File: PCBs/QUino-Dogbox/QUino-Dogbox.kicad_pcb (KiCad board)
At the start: 2 copper layers, 77.5 x 64.8 mm, 70 parts, among them IC1 TP5000-QFN16, J1 RFID RC522, J2 Micro_SD_Card, J3 Neopixel, J4 USB_B_Micro, J5 Conn_01x07_Male, Q1 Q12MHz/20pF/10ppm/4P/3.2x2.5mm, Q2 BC817-40(SOT23), Q3 BC817-40(SOT23), Q4 SI2302DS NMOS/GSD, Q5 QBC817 NPN/BEC, U1 ESP32-S2-WROVER, U3 CH340T(SSOP20W), U4 AMS1117-3.3

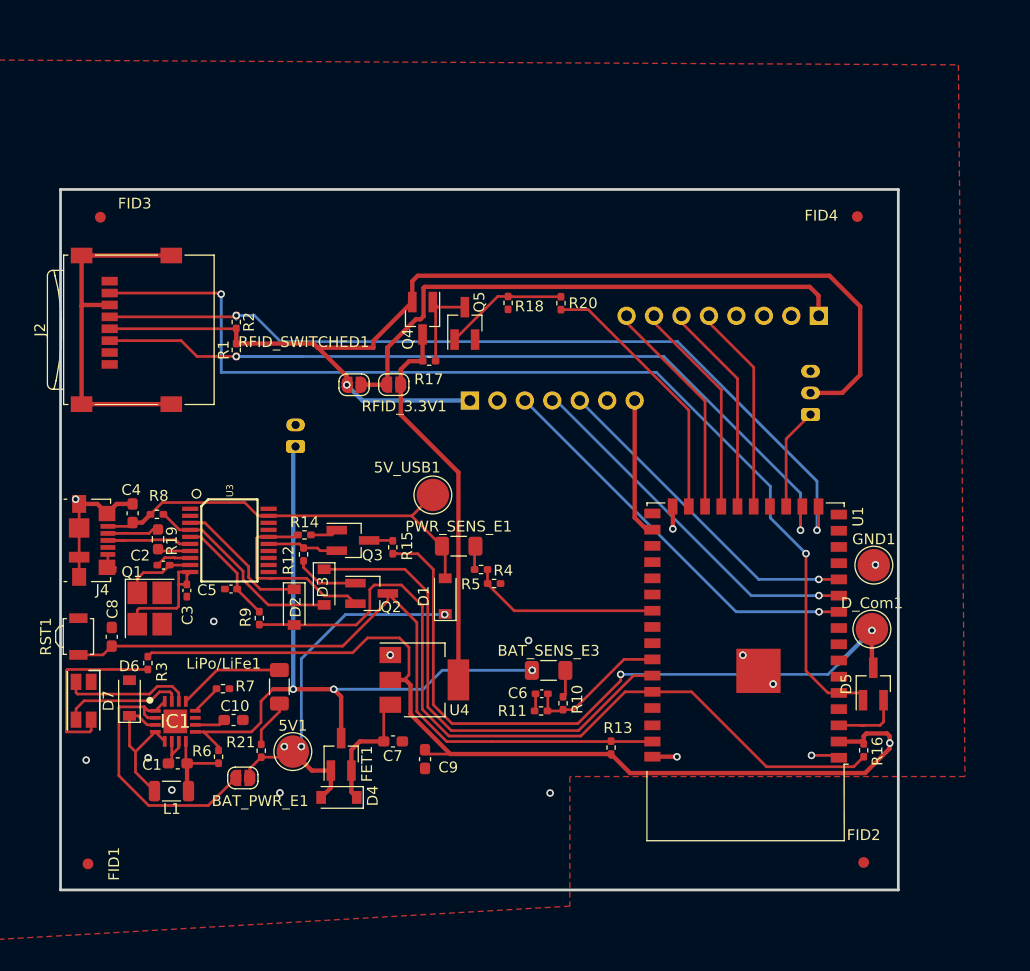
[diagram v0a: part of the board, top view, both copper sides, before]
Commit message: Update ESP32 to WROVER-B
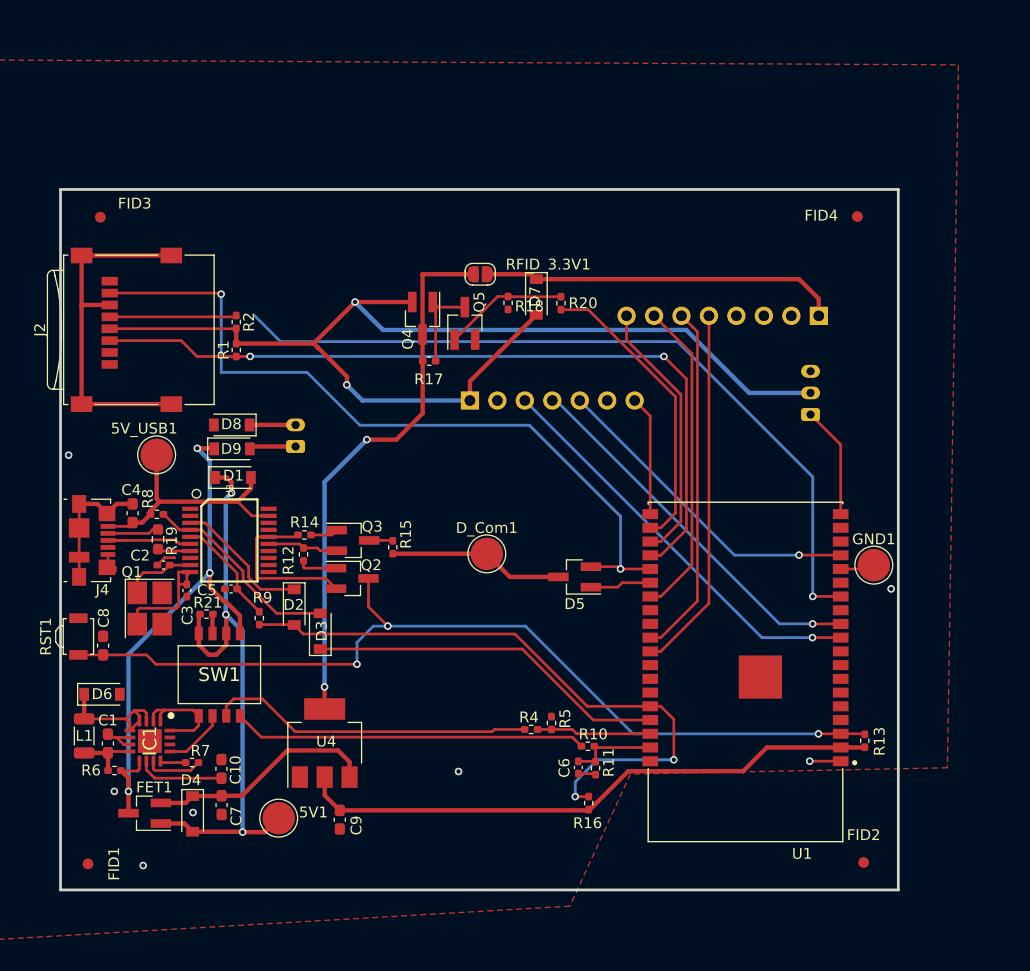
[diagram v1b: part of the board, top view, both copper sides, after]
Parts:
- removed BAT_PWR_E1, RFID_SWITCHED1: Opened, Jumper:SolderJumper-2_P1.3mm_Open_RoundedPad1.0x1.5mm
- removed BAT_SENS_E3, LiPo/LiFe1, PWR_SENS_E1: Opened, Resistor_SMD:R_1206_3216Metric_Pad1.30x1.75mm_HandSolder
- removed R3: 1k/R0402, Resistor_SMD:R_0402_1005Metric_Pad0.72x0.64mm_HandSolder
- added D8: 1N5819W/SOD123, Diode_SMD:D_SOD-123, F.Cu at (102.8, 98.5)
- added D9: 1N5819W/SOD123, Diode_SMD:D_SOD-123, F.Cu at (102.9, 100.7)
- added SW1: SW_DIP_x04, ProjectLib:DSHP04TSS, F.Cu at (101.7, 121.6)
- D1, D2, D3, D4, D6: value 1N5819S4/SOD123 -> 1N5819W/SOD123
- D7: value LED_RGBA -> 1N5819W/SOD123; footprint LED_SMD:LED_RGB_1210 -> Diode_SMD:D_SOD-123
- R15: value 220R/R0402 -> 220/R0402
- R16: value NA/R0402 -> 10k/R0402
- U1: value ESP32-S2-WROVER -> ESP32-WROVER; footprint RF_Module:ESP32-S2-WROVER -> ESP32-DevKit-LiPo-Rev:XCVR_ESP32-WROVER-I
- moved D7 56.1 mm to (131.0, 86.6)
- moved D_Com1 36.3 mm to (126.4, 110.4)
- moved D5 29.3 mm to (134.6, 112.5), turned to 180 degrees
- moved R16 25.9 mm to (135.9, 133.4), turned to 270 degrees
- moved 5V_USB1 25.8 mm to (95.9, 101.2)
- moved R13 23.5 mm to (161.4, 127.7)
- moved D1 22.5 mm to (103.0, 103.3), turned to 0 degrees
- moved FET1 19.0 mm to (94.8, 134.4), turned to 180 degrees
- moved C7 16.9 mm to (101.9, 133.6), turned to 270 degrees
- moved R4 15.5 mm to (130.5, 126.6)
- moved R5 14.0 mm to (132.4, 126.0), turned to 270 degrees
- moved D4 13.6 mm to (99.2, 134.4), turned to 270 degrees
- moved R21 13.6 mm to (100.5, 116.0), turned to 0 degrees
- moved RFID_3.3V1 13.0 mm to (125.8, 84.5), turned to 0 degrees
- moved U4 10.9 mm to (111.4, 127.9), turned to 90 degrees
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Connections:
- BAT1 pad 1: VBAT -> Net-(BAT1-Pad1)
- BAT1 pad 2: GND -> Net-(BAT1-Pad2)
- D5 pad 1: GPIO_2 -> GPIO_0
- D5 pad 2: GPIO_0 -> GPIO_2
- D7 pad 1: /LiPoPower/LOWPWR_LED -> Net-(D7-Pad1)
- D7 pad 2: Net-(D7-Pad2) -> /VSwitched
- IC1 pad 14: Net-(D7-Pad2) -> Net-(IC1-Pad14)
- IC1 pad 15: Net-(D7-Pad3) -> Net-(IC1-Pad15)
- J1 pad 1: Net-(J1-Pad1) -> Net-(D7-Pad1)
- R5 pad 1: EXTPWR_SENSE -> GND
- R5 pad 2: GND -> EXTPWR_SENSE
- RFID_3.3V1 pad 2: Net-(J1-Pad1) -> Net-(D7-Pad1)
- U1 pad 12: DAC_CLK -> Net-(U1-Pad12)
- U1 pad 13: Net-(U1-Pad13) -> GPIO_14
- U1 pad 15: Net-(U1-Pad15) -> GND
- U1 pad 16: Net-(U1-Pad16) -> DAC_CLK
- U1 pad 17: GPIO_14 -> Net-(U1-Pad17)
- U1 pad 18: GPIO_15 -> Net-(U1-Pad18)
- U1 pad 20: Net-(U1-Pad20) -> HEADPHONE_JACK
- U1 pad 21: RFID_MISO -> GATE_PWR
- U1 pad 22: RFID_MOSI -> RFID_CS
- U1 pad 23: RFID_CLK -> GPIO_15
- U1 pad 24: RFID_CS -> GPIO_2
- U1 pad 25: GATE_PWR -> GPIO_0
- U1 pad 26: GND -> RFID_CLK
- U1 pad 27: Net-(U1-Pad27) -> (no net)
- U1 pad 28: HEADPHONE_JACK -> (no net)
- U1 pad 29: Net-(U1-Pad29) -> RFID_MOSI
- U1 pad 3: GPIO_0 -> /Sheet602F0C3C/GPIO_EN
- U1 pad 30: Net-(U1-Pad30) -> RFID_MISO
- U1 pad 32: Net-(U1-Pad32) -> (no net)
- U1 pad 33: EXTPWR_SENSE -> Net-(U1-Pad33)
- U1 pad 34: Net-(U1-Pad34) -> GPIO_RX
- U1 pad 35: Net-(U1-Pad35) -> GPIO_TX
- U1 pad 36: VBAT_MEASURE -> EXTPWR_SENSE
- U1 pad 37: GPIO_TX -> VBAT_MEASURE
- U1 pad 38: GPIO_RX -> GND
- U1 pad 5: GPIO_2 -> Net-(U1-Pad5)
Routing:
- net Net-(J1-Pad1): track 53.1 -> 0.00 mm
- net /Sheet602F0C3C/D_Com: track 66.0 -> 16.2 mm, vias 2 -> 0
- net Net-(D7-Pad1): track 0.00 -> 33.2 mm
- net Net-(R10-Pad1): track 2.53 -> 32.7 mm
- net Net-(R4-Pad2): track 2.19 -> 30.1 mm
- net GPIO_2: track 97.9 -> 70.5 mm
- net +3V3: track 127.4 -> 104.9 mm, vias 1 -> 2
- net /Sheet602F0C3C/GPIO_EN: track 67.7 -> 85.6 mm, vias 0 -> 3
- net +5V: track 38.4 -> 55.7 mm
- net GPIO_RX: track 75.4 -> 58.3 mm, vias 0 -> 2
- net Net-(D7-Pad4): track 16.6 -> 0.00 mm
- net Net-(IC1-Pad1): track 25.9 -> 10.2 mm
- net /LiPoPower/5V: track 39.4 -> 23.7 mm
- net RFID_MISO: track 18.8 -> 33.9 mm
- net VBAT: track 64.7 -> 50.6 mm
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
